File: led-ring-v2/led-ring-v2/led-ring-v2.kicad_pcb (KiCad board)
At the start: 2 copper layers, 54.9 x 54.9 mm, 43 parts, among them J1 Conn_01x02_Pin

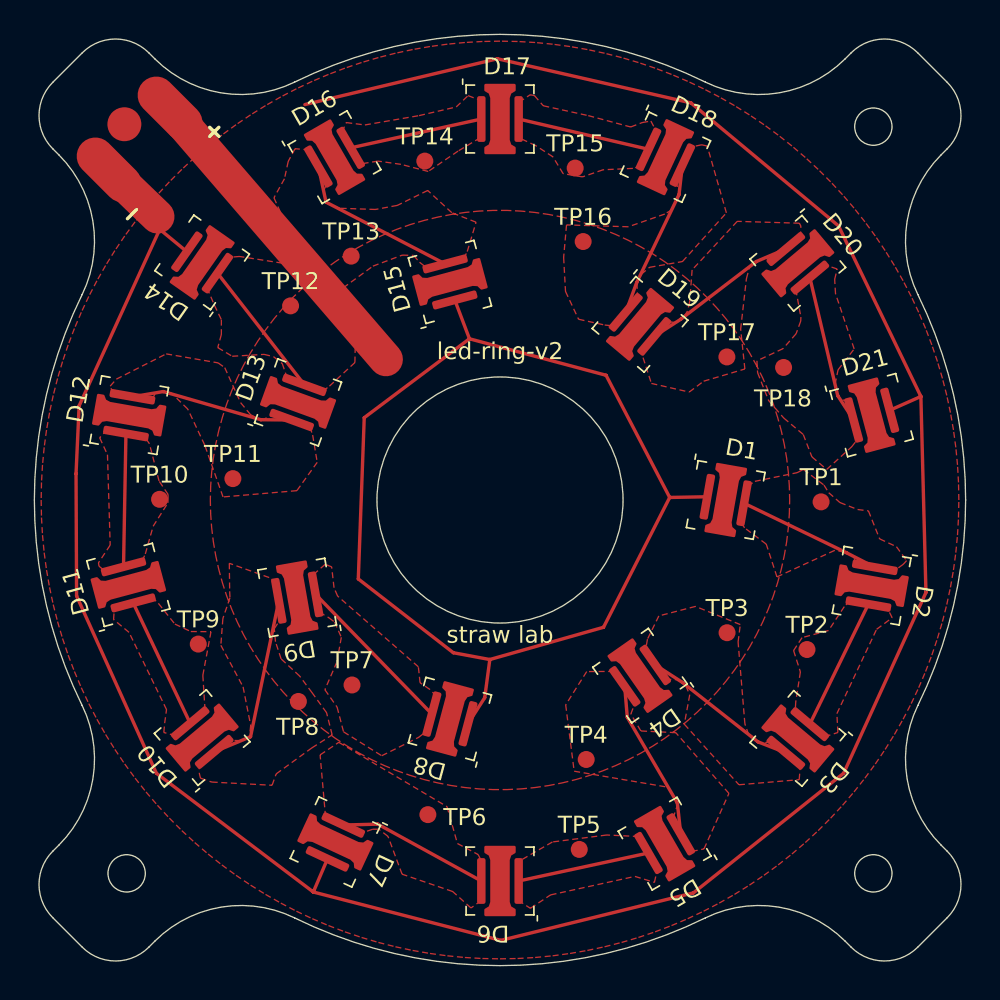
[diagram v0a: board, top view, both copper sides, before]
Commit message: led-ring-v2.1
* fix polarity markings
* add lens circles to aid glue deposition
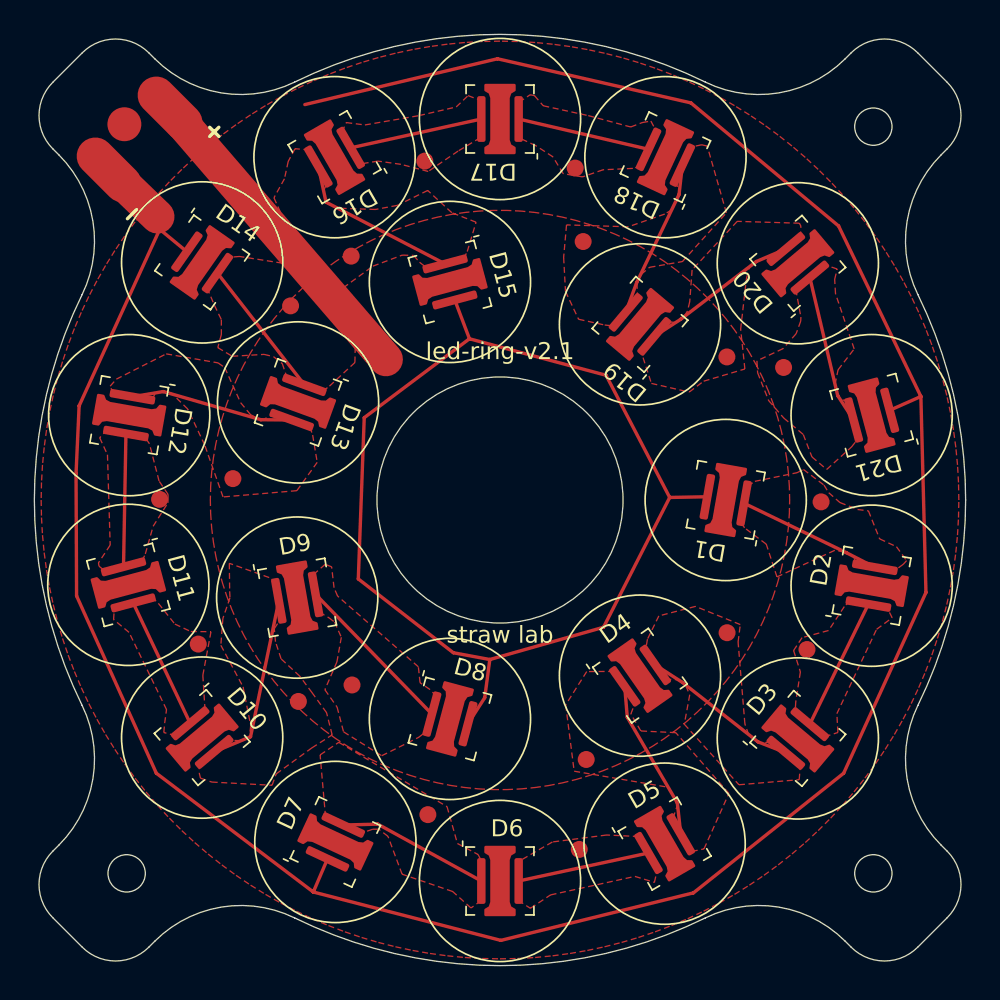
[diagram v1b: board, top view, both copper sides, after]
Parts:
- D1, D10, D11, D12, D13, D14, D15, D16, D17, D18, D19, D2, D20, D21, D3, D4, D5, D6, D7, D8, D9: footprint victor_strawlab:OSRAM_SFH_4715AS -> victor_strawlab:OSRAM_SFH_4715AS_with_LISA4
- turned D1 to 80 degrees
- turned D10 to -140 degrees
- turned D11 to -165 degrees
- turned D12 to 170 degrees
- turned D13 to 160 degrees
- turned D14 to -125 degrees
- turned D15 to -165 degrees
- turned D16 to 120 degrees
- turned D17 to 90 degrees
- turned D18 to 65 degrees
- turned D19 to 50 degrees
- turned D2 to -10 degrees
- turned D20 to 40 degrees
- turned D21 to 105 degrees
- turned D3 to -40 degrees
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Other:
- board text added: "led-ring-v2.1"
- board text removed: "led-ring-v2"
